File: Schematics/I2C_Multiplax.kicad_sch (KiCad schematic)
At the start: 0 parts

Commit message: Fixed bugs in voice selection on configuration.  Reorganized schematics to have different master drawings for power and audio paths.  Started work on dual 3-pole state variable filter with resonance.
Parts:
- added C427, C441: 10µF, symbol Device:C_Polarized_Small_US
- added C431, C445: 0.1µF, symbol Device:C_Small
- added J46, J47, J48, J49, J50, J51, J52, J53: Conn_01x04, symbol Connector_keyed_kicad_sym:Conn_01x04
- added R29, R30, R31: 10k, symbol Device:R_Small_US
- added U207, U208, U209: TCA9548A, Package_SO:SOIC-24W_7.5x15.4mm_P1.27mm, symbol Interface_Expansion:PCA9548ADW
- added U276: LM1117-3.3, symbol Regulator_Linear:LM1117-3.3
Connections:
- new net: J46.2 (Pin_2), U207.16 (SD0)
- new net: J46.3 (Pin_3), U207.15 (SC0)
- new net: R31.2, U207.20 (~{RESET})
- new net: J52.2 (Pin_2), U207.4 (SD6)
- new net: J52.3 (Pin_3), U207.3 (SC6)
- new net: J51.2 (Pin_2), U207.6 (SD5)
- new net: J51.3 (Pin_3), U207.5 (SC5)
- new net: J53.3 (Pin_3), U207.1 (SC7)
- new net: J49.2 (Pin_2), U207.10 (SD3)
- new net: J48.3 (Pin_3), U207.11 (SC2)
- new net: J48.2 (Pin_2), U207.12 (SD2)
- new net: J47.3 (Pin_3), U207.13 (SC1)
- new net: J47.2 (Pin_2), U207.14 (SD1)
- new net: J53.2 (Pin_2), U207.2 (SD7)
- new net: J50.3 (Pin_3), U207.7 (SC4)
- new net: J50.2 (Pin_2), U207.8 (SD4)
- new net: J49.3 (Pin_3), U207.9 (SC3)
- new net: C441.1, C445.1, U276.2 (VO)
- new net: R29.1, R30.1, U208.17 (A2), U208.24 (VCC), U209.17 (A2), U209.19 (A0), U209.24 (VCC)
- new net: R29.2, U209.20 (~{RESET})
- new net: R30.2, U208.20 (~{RESET})
- new net +3V3: R31.1, U207.18 (A1), U207.19 (A0), U207.24 (VCC)
- new net +5D: C427.1, C431.1, U276.3 (VI)
- new net GND1: C427.2, C431.2, C441.2, C445.2, U207.17 (A2), U207.23 (GND), U208.18 (A1), U208.19 (A0), U208.23 (GND), U209.18 (A1), U209.23 (GND), U276.1 (GND)
- new net SCL0: U207.21 (SCL), U208.21 (SCL), U209.21 (SCL)
- new net SDA0: U207.22 (SDA), U208.22 (SDA), U209.22 (SDA)

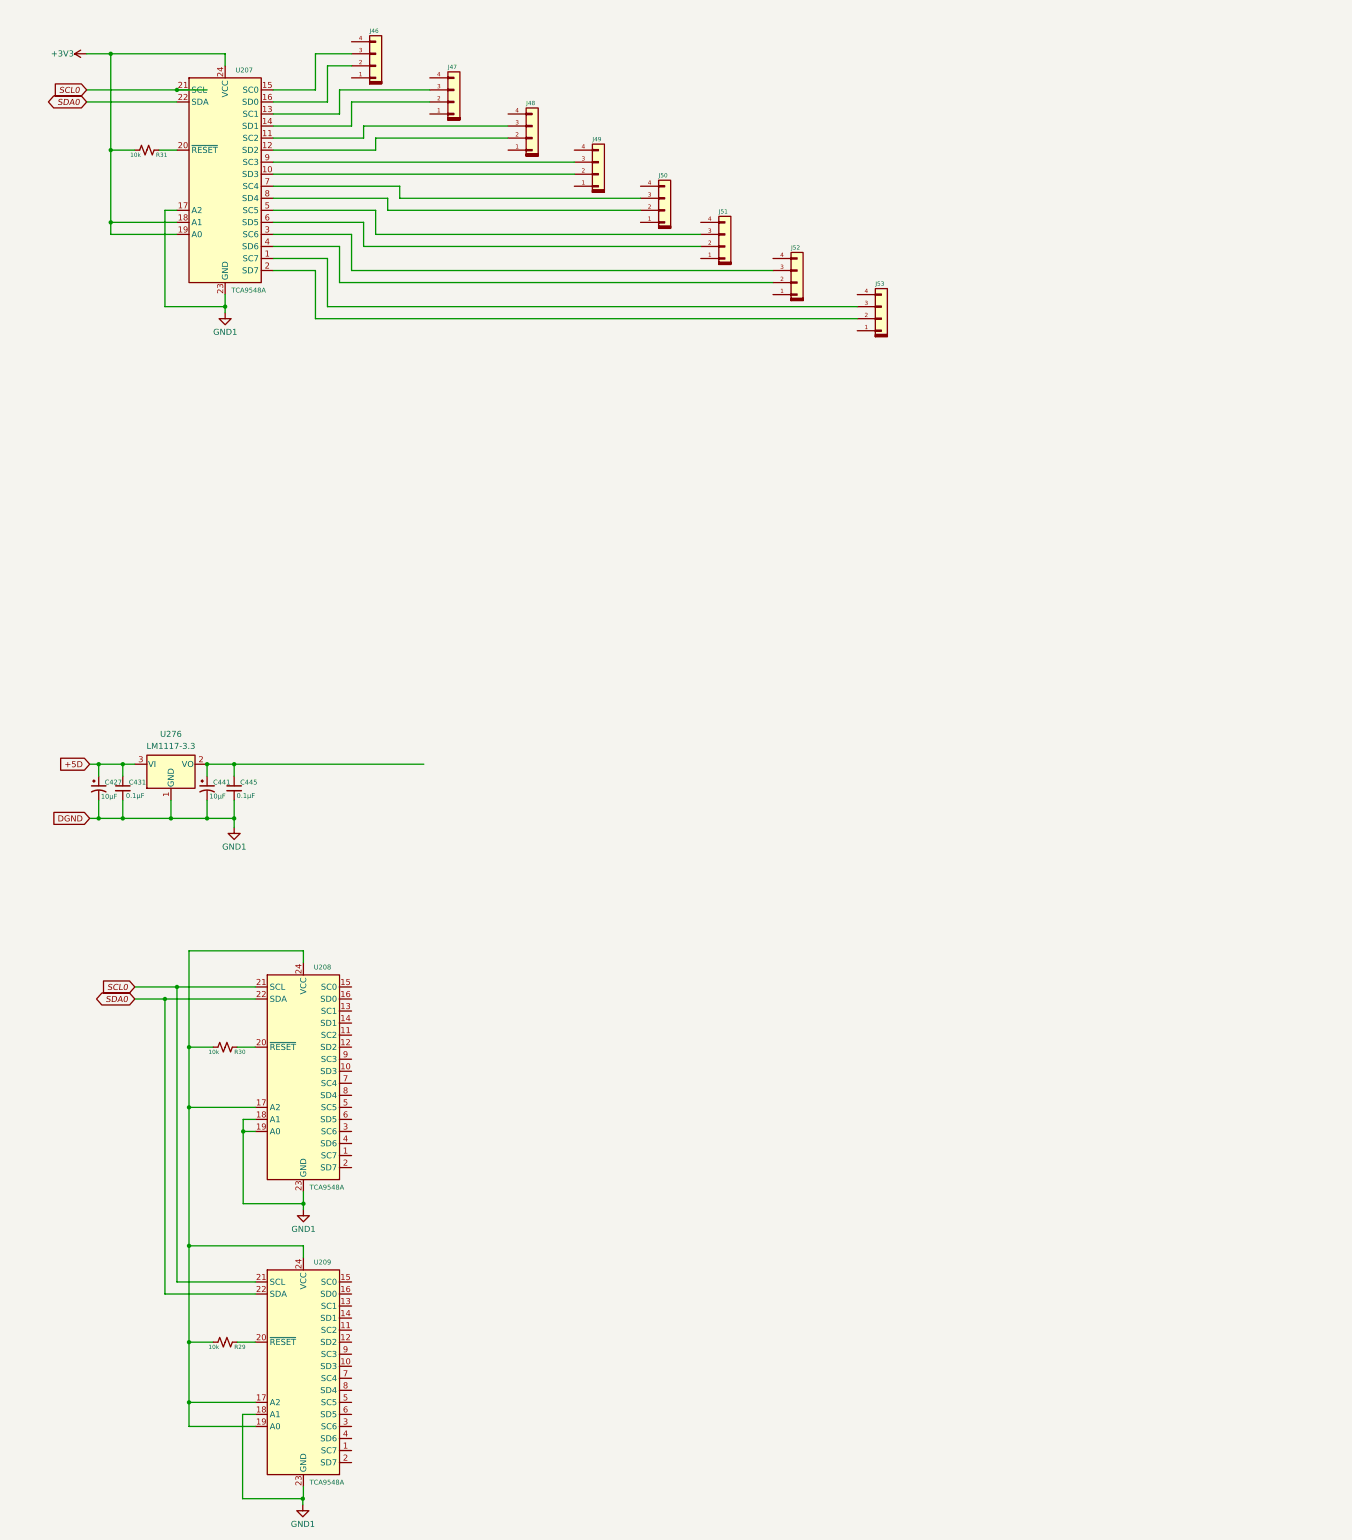
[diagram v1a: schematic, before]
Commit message: Fixed schematic errors.
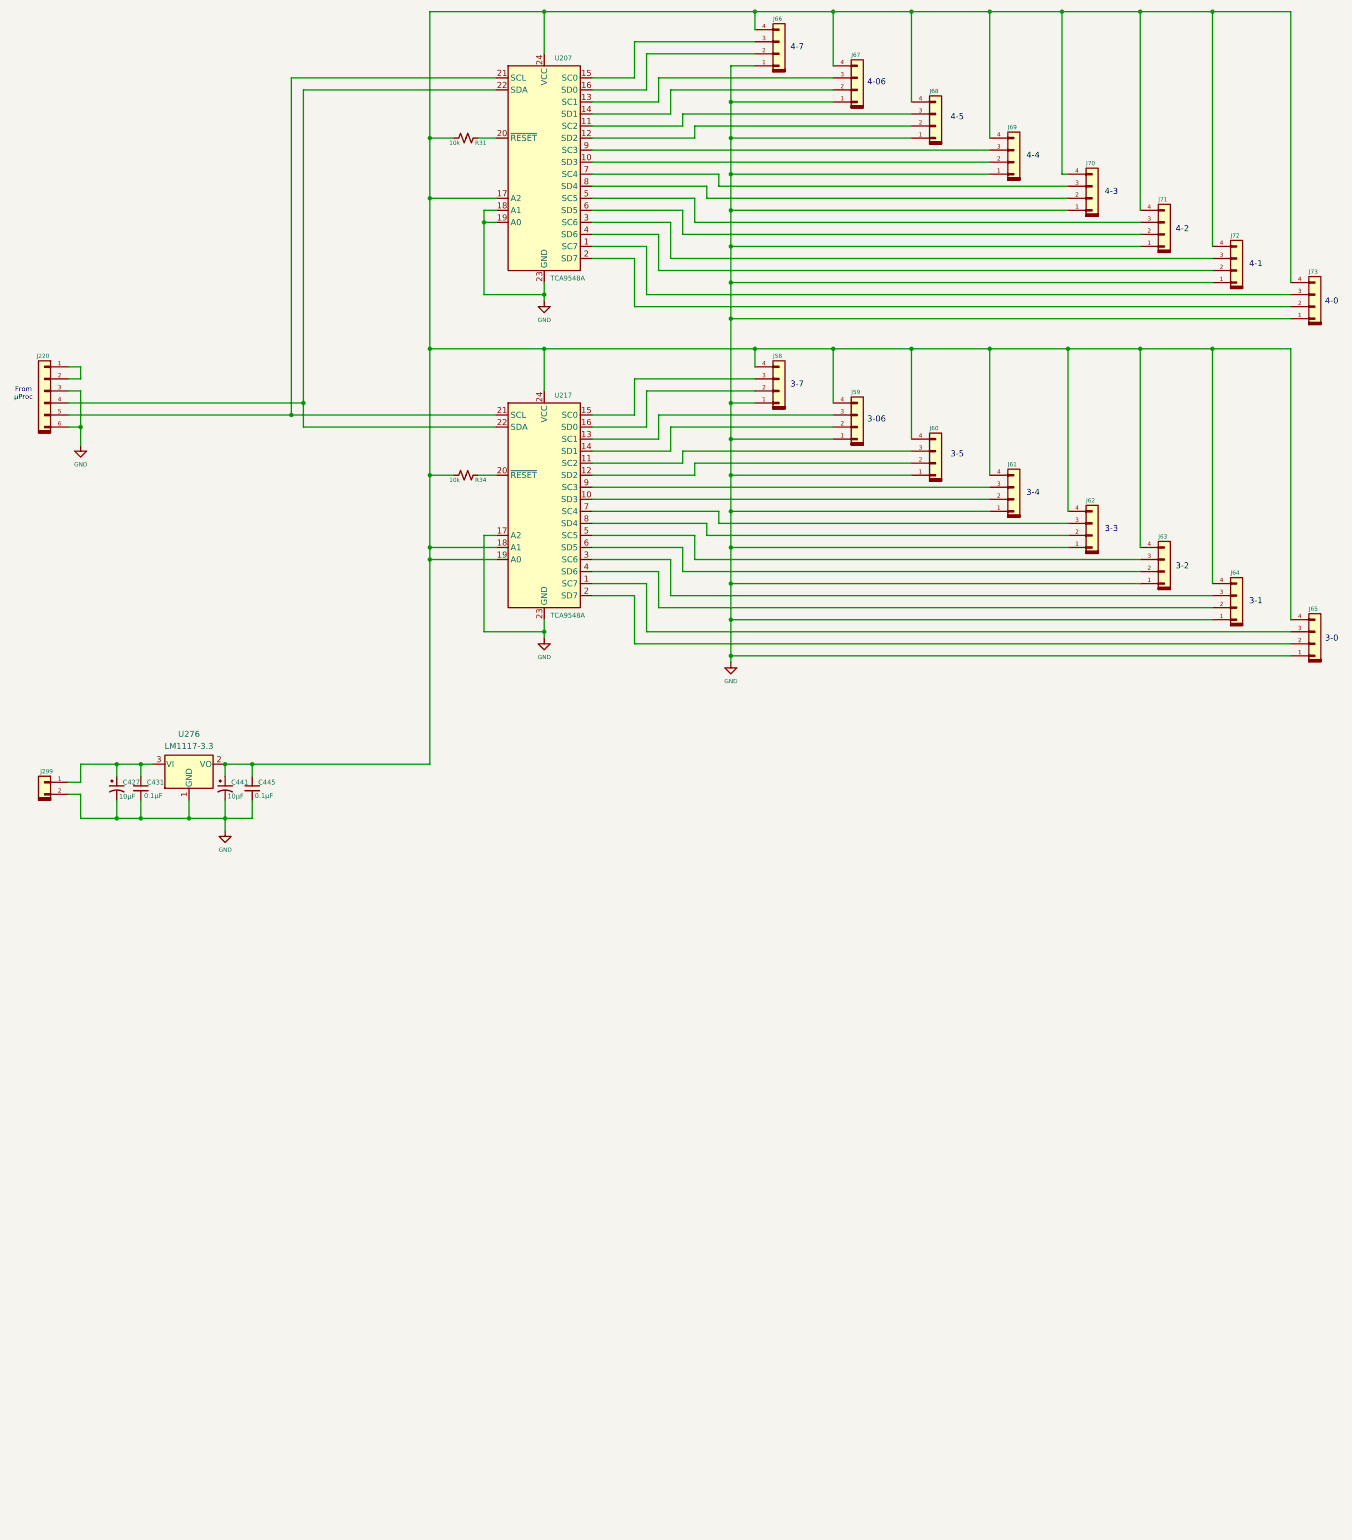
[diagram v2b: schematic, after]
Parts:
- removed J46, J47, J48, J49, J50, J51, J52, J53: Conn_01x04, symbol Connector_keyed_kicad_sym:Conn_01x04
- removed R29, R30: 10k, symbol Device:R_Small_US
- removed U208, U209: TCA9548A, Package_SO:SOIC-24W_7.5x15.4mm_P1.27mm, symbol Interface_Expansion:PCA9548ADW
- added J220: Conn_01x06, symbol My Connectors:Conn_01x06
- added J299: Conn_01x02, symbol My Connectors:Conn_01x02
- added J58, J59, J60, J61, J62, J63, J64, J65, J66, J67, J68, J69, J70, J71, J72, J73: Conn_01x04, symbol Connector_keyed_kicad_sym:Conn_01x04
- added R34: 10k, symbol Device:R_Small_US
- added U217: TCA9548A, Package_SO:SOIC-24W_7.5x15.4mm_P1.27mm, symbol Interface_Expansion:PCA9548ADW
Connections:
- net at U207.16 (SD0): now also J66.2 (Pin_2)
- net at U207.15 (SC0): now also J66.3 (Pin_3)
- net at U207.4 (SD6): now also J72.2 (Pin_2)
- net at U207.3 (SC6): now also J72.3 (Pin_3)
- net at U207.6 (SD5): now also J71.2 (Pin_2)
- net at U207.5 (SC5): now also J71.3 (Pin_3)
- net at U207.1 (SC7): now also J73.3 (Pin_3)
- net at U207.10 (SD3): now also J69.2 (Pin_2)
- net at U207.11 (SC2): now also J68.3 (Pin_3)
- net at U207.12 (SD2): now also J68.2 (Pin_2)
- net at U207.13 (SC1): now also J67.3 (Pin_3)
- net at U207.14 (SD1): now also J67.2 (Pin_2)
- net at U207.2 (SD7): now also J73.2 (Pin_2)
- net at U207.7 (SC4): now also J70.3 (Pin_3)
- net at U207.8 (SD4): now also J70.2 (Pin_2)
- net at U207.9 (SC3): now also J69.3 (Pin_3)
- net at C441.1, C445.1, U276.2 (VO): now also R31.1, U207.17 (A2), U207.24 (VCC), J58.4 (Pin_4), J59.4 (Pin_4), J60.4 (Pin_4), J61.4 (Pin_4), J62.4 (Pin_4), J63.4 (Pin_4), J64.4 (Pin_4), J65.4 (Pin_4), J66.4 (Pin_4), J67.4 (Pin_4), J68.4 (Pin_4), J69.4 (Pin_4), J70.4 (Pin_4), J71.4 (Pin_4), J72.4 (Pin_4), J73.4 (Pin_4), R34.1, U217.18 (A1), U217.19 (A0), U217.24 (VCC)
- net +3V3 renamed GND
- net GND: now also C427.2, C431.2, C441.2, C445.2, U207.23 (GND), U276.1 (GND), J220.3 (Pin_3), J220.6 (Pin_6), J299.2 (Pin_2), J58.1 (Pin_1), J59.1 (Pin_1), J60.1 (Pin_1), J61.1 (Pin_1), J62.1 (Pin_1), J63.1 (Pin_1), J64.1 (Pin_1), J65.1 (Pin_1), J66.1 (Pin_1), J67.1 (Pin_1), J68.1 (Pin_1), J69.1 (Pin_1), J70.1 (Pin_1), J71.1 (Pin_1), J72.1 (Pin_1), J73.1 (Pin_1), U217.17 (A2), U217.23 (GND); no longer R31.1, U207.24 (VCC)
- net +5D: no longer names the net of C427.1, C431.1, U276.3 (VI)
- net +5D: now also J299.1 (Pin_1)
- removed net GND1: C427.2, C431.2, C441.2, C445.2, U207.17 (A2), U207.23 (GND), U276.1 (GND)
- net SCL0: no longer names the net of U207.21 (SCL)
- net SCL0: now also J220.5 (Pin_5), U217.21 (SCL)
- net SDA0: no longer names the net of U207.22 (SDA)
- net SDA0: now also J220.4 (Pin_4), U217.22 (SDA)
- new net: R34.2, U217.20 (~{RESET})
- new net: J65.3 (Pin_3), U217.1 (SC7)
- new net: J61.2 (Pin_2), U217.10 (SD3)
- new net: J60.3 (Pin_3), U217.11 (SC2)
- new net: J60.2 (Pin_2), U217.12 (SD2)
- new net: J59.3 (Pin_3), U217.13 (SC1)
- new net: J59.2 (Pin_2), U217.14 (SD1)
- new net: J58.3 (Pin_3), U217.15 (SC0)
- new net: J58.2 (Pin_2), U217.16 (SD0)
- new net: J65.2 (Pin_2), U217.2 (SD7)
- new net: J64.3 (Pin_3), U217.3 (SC6)
- new net: J64.2 (Pin_2), U217.4 (SD6)
- new net: J63.3 (Pin_3), U217.5 (SC5)
- new net: J63.2 (Pin_2), U217.6 (SD5)
- new net: J62.3 (Pin_3), U217.7 (SC4)
- new net: J62.2 (Pin_2), U217.8 (SD4)
- new net: J61.3 (Pin_3), U217.9 (SC3)
- new net: J220.1 (Pin_1), J220.2 (Pin_2)
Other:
- note added: "3-0"
- note added: "3-06"
- note added: "3-1"
- note added: "3-2"
- note added: "3-3"
- note added: "3-4"
- note added: "3-5"
- note added: "3-7"
- note added: "4-0"
- note added: "4-06"
- note added: "4-1"
- note added: "4-2"
- note added: "4-3"
- note added: "4-4"
- note added: "4-5"
- note added: "4-7"
- note added: "From µProc"
- moved on the sheet: C427, C431, C441, C445, R31, U207, U276

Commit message: Refactored hardware and software.  Improved Launch Control XL configuration and control.
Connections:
- net GND: now also U207.17 (A2), U217.18 (A1), U217.19 (A0); no longer U207.19 (A0)
- net at C441.1, C445.1, J58.4 (Pin_4)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: no longer U207.17 (A2), U217.18 (A1), U217.19 (A0)
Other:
- note added: "0-0"
- note added: "0-1"
- note added: "0-2"
- note added: "0-3"
- note added: "0-4"
- note added: "0-5"
- note added: "0-6"
- note added: "0-7"
- note added: "1-0"
- note added: "1-1"
- note added: "1-2"
- note added: "1-3"
- note added: "1-4"
- note added: "1-5"
- note added: "1-6"
- note added: "1-7"
- note added: "Cluster #0"
- note added: "Cluster #1"
- note removed: "3-0"
- note removed: "3-06"
- note removed: "3-1"
- note removed: "3-2"
- note removed: "3-3"
- note removed: "3-4"
- note removed: "3-5"
- note removed: "3-7"
- note removed: "4-0"
- note removed: "4-06"
- note removed: "4-1"
- note removed: "4-2"
- note removed: "4-3"
- note removed: "4-4"
- note removed: "4-5"
- note removed: "4-7"
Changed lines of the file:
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@@
 	(generator_version "9.0")
 	(paper "USLegal")
-	(text "3-0"
+	(text "0-0"
 		(exclude_from_sim no)
 		(at 291.846 152.654 0)
@@
 		)
 	)
-	(text "4-3"
+	(text "Cluster #0"
+		(exclude_from_sim no)
+		(at 87.122 119.888 0)
+		(effects
+			(font
+				(face "Bahnschrift")
+				(size 1.6256 1.6256)
+			)
+		)
+	)
+	(text "1-3"
 		(exclude_from_sim no)
 		(at 245.364 58.42 0)
@@
 		)
 	)
-	(text "3-3"
+	(text "0-3"
 		(exclude_from_sim no)
 		(at 245.364 129.54 0)
@@
 		)
 	)
-	(text "4-06"
+	(text "1-6"
 		(exclude_from_sim no)
 		(at 195.834 35.306 0)
@@
 		)
 	)
-	(text "3-06"
+	(text "0-6"
 		(exclude_from_sim no)
 		(at 195.834 106.426 0)
@@
 		)
 	)
-	(text "4-2"
+	(text "1-2"
 		(exclude_from_sim no)
 		(at 260.35 66.294 0)
@@
 		)
 	)
-	(text "3-7"
+	(text "0-7"
 		(exclude_from_sim no)
 		(at 179.07 99.06 0)
@@
 		)
 	)
-	(text "4-0"
+	(text "Cluster #1"
+		(exclude_from_sim no)
+		(at 87.122 48.768 0)
+		(effects
+			(font
+				(face "Bahnschrift")
+				(size 1.6256 1.6256)
+			)
+		)
+	)
+	(text "1-0"
 		(exclude_from_sim no)
 		(at 291.846 81.534 0)
@@
 		)
 	)
-	(text "3-2"
+	(text "0-2"
 		(exclude_from_sim no)
 		(at 260.35 137.414 0)
@@
 		)
 	)
-	(text "4-7"
+	(text "1-7"
 		(exclude_from_sim no)
 		(at 179.07 27.94 0)
@@
 		)
 	)
-	(text "4-1"
+	(text "1-1"
 		(exclude_from_sim no)
 		(at 275.844 73.66 0)
@@
 		)
 	)
-	(text "4-4"
+	(text "1-4"
 		(exclude_from_sim no)
 		(at 228.854 50.8 0)
@@
 		)
 	)
-	(text "3-4"
+	(text "0-4"
 		(exclude_from_sim no)
 		(at 228.854 121.92 0)
@@
 		)
 	)
-	(text "3-1"
+	(text "0-1"
 		(exclude_from_sim no)
 		(at 275.844 144.78 0)
@@
 		)
 	)
-	(text "4-5"
+	(text "1-5"
 		(exclude_from_sim no)
 		(at 212.852 42.672 0)
@@
 		)
 	)
-	(text "3-5"
+	(text "0-5"
 		(exclude_from_sim no)
 		(at 212.852 113.792 0)
@@
 	)
 	(junction
-		(at 101.6 135.89)
-		(diameter 0)
-		(color 0 0 0 0)
-	)
-	(junction
 		(at 165.1 54.61)
 		(diameter 0)
@@
 	)
 	(junction
-		(at 113.03 64.77)
-		(diameter 0)
-		(color 0 0 0 0)
-	)
-	(junction
-		(at 101.6 59.69)
+		(at 113.03 135.89)
 		(diameter 0)
 		(color 0 0 0 0)
@@
 	)
 	(junction
+		(at 113.03 62.23)
+		(diameter 0)
+		(color 0 0 0 0)
+	)
+	(junction
 		(at 165.1 102.87)
 		(diameter 0)
@@
 	)
 	(junction
-		(at 101.6 133.35)
-		(diameter 0)
-		(color 0 0 0 0)
-	)
-	(junction
 		(at 165.1 118.11)
 		(diameter 0)
@@
 	)
 	(junction
+		(at 113.03 133.35)
+		(diameter 0)
+		(color 0 0 0 0)
+	)
+	(junction
 		(at 101.6 91.44)
 		(diameter 0)
@@
 	(wire
 		(pts
+			(xy 113.03 62.23) (xy 115.57 62.23)
+		)
+		(stroke
+			(width 0)
+			(type default)
+		)
+	)
+	(wire
+		(pts
 			(xy 35.56 190.5) (xy 35.56 186.69)
 		)
@@
 	(wire
 		(pts
-			(xy 113.03 62.23) (xy 113.03 64.77)
-		)
-		(stroke
-			(width 0)
-			(type default)
-		)
-	)
-	(wire
-		(pts
 			(xy 186.69 34.29) (xy 149.86 34.29)
 		)
@@
 	(wire
 		(pts
+			(xy 113.03 59.69) (xy 115.57 59.69)
+		)
+		(stroke
+			(width 0)
+			(type default)
+		)
+	)
+	(wire
+		(pts
 			(xy 50.8 190.5) (xy 58.42 190.5)
 		)
@@
 	(wire
 		(pts
-			(xy 101.6 135.89) (xy 115.57 135.89)
-		)
-		(stroke
-			(width 0)
-			(type default)
-		)
-	)
-	(wire
-		(pts
 			(xy 251.46 20.32) (xy 266.7 20.32)
 		)
@@
 	(wire
 		(pts
-			(xy 113.03 130.81) (xy 113.03 151.13)
+			(xy 113.03 130.81) (xy 113.03 133.35)
 		)
 		(stroke
@@
 	(wire
 		(pts
+			(xy 113.03 133.35) (xy 113.03 135.89)
+		)
+		(stroke
+			(width 0)
+			(type default)
+		)
+	)
+	(wire
+		(pts
 			(xy 266.7 143.51) (xy 152.4 143.51)
 		)
@@
 	(wire
 		(pts
-			(xy 101.6 59.69) (xy 101.6 91.44)
-		)
-		(stroke
-			(width 0)
-			(type default)
-		)
-	)
-	(wire
-		(pts
 			(xy 165.1 46.99) (xy 203.2 46.99)
 		)
@@
 	(wire
 		(pts
-			(xy 101.6 133.35) (xy 115.57 133.35)
-		)
-		(stroke
-			(width 0)
-			(type default)
-		)
-	)
-	(wire
-		(pts
 			(xy 157.48 44.45) (xy 203.2 44.45)
 		)
@@
 	(wire
 		(pts
-			(xy 113.03 64.77) (xy 113.03 80.01)
+			(xy 113.03 59.69) (xy 113.03 62.23)
 		)
 		(stroke
@@
 	(wire
 		(pts
-			(xy 115.57 62.23) (xy 113.03 62.23)
-		)
-		(stroke
-			(width 0)
-			(type default)
-		)
-	)
-	(wire
-		(pts
 			(xy 165.1 85.09) (xy 283.21 85.09)
 		)
@@
 	(wire
 		(pts
-			(xy 101.6 133.35) (xy 101.6 135.89)
+			(xy 101.6 118.11) (xy 101.6 179.07)
 		)
 		(stroke
@@
 	(wire
 		(pts
+			(xy 113.03 62.23) (xy 113.03 80.01)
+		)
+		(stroke
+			(width 0)
+			(type default)
+		)
+	)
+	(wire
+		(pts
 			(xy 154.94 113.03) (xy 203.2 113.03)
 		)
@@
 	(wire
 		(pts
+			(xy 113.03 135.89) (xy 113.03 151.13)
+		)
+		(stroke
+			(width 0)
+			(type default)
+		)
+	)
+	(wire
+		(pts
 			(xy 135.89 72.39) (xy 144.78 72.39)
 		)
@@
 	(wire
 		(pts
-			(xy 101.6 46.99) (xy 101.6 59.69)
+			(xy 101.6 46.99) (xy 101.6 91.44)
+		)
+		(stroke
+			(width 0)
+			(type default)
+		)
+	)
+	(wire
+		(pts
+			(xy 113.03 133.35) (xy 115.57 133.35)
 		)
 		(stroke
@@
 	(wire
 		(pts
-			(xy 101.6 118.11) (xy 101.6 133.35)
-		)
-		(stroke
-			(width 0)
-			(type default)
-		)
-	)
-	(wire
-		(pts
 			(xy 283.21 91.44) (xy 266.7 91.44)
 		)
@@
 	(wire
 		(pts
-			(xy 101.6 59.69) (xy 115.57 59.69)
-		)
-		(stroke
-			(width 0)
-			(type default)
-		)
-	)
-	(wire
-		(pts
 			(xy 162.56 125.73) (xy 135.89 125.73)
 		)
@@
 	(wire
 		(pts
+			(xy 113.03 135.89) (xy 115.57 135.89)
+		)
+		(stroke
+			(width 0)
+			(type default)
+		)
+	)
+	(wire
+		(pts
 			(xy 58.42 190.5) (xy 58.42 193.04)
 		)
@@
 	(wire
 		(pts
-			(xy 101.6 135.89) (xy 101.6 179.07)
-		)
-		(stroke
-			(width 0)
-			(type default)
-		)
-	)
-	(wire
-		(pts
 			(xy 135.89 133.35) (xy 154.94 133.35)
 		)
@@
 	(wire
 		(pts
-			(xy 113.03 64.77) (xy 115.57 64.77)
-		)
-		(stroke
-			(width 0)
-			(type default)
-		)
-	)
-	(wire
-		(pts
 			(xy 186.69 91.44) (xy 186.69 102.87)
 		)
 		(stroke
+			(width 0)
+			(type default)
+		)
+	)
+	(wire
+		(pts
+			(xy 100.33 64.77) (xy 115.57 64.77)
+		)
+		(stroke
